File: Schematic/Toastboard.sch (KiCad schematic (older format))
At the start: 46 parts, among them J1 Conn_01x20_Female, J2 USB_B_Micro, Q1 FDS6892A, SW1 SW_Push, SW2 SW_Push, SW3 SW_Push, SW4 SW_Push, SW5 SW_DIP_x04, U1 24LC01, U2 PCT2075D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

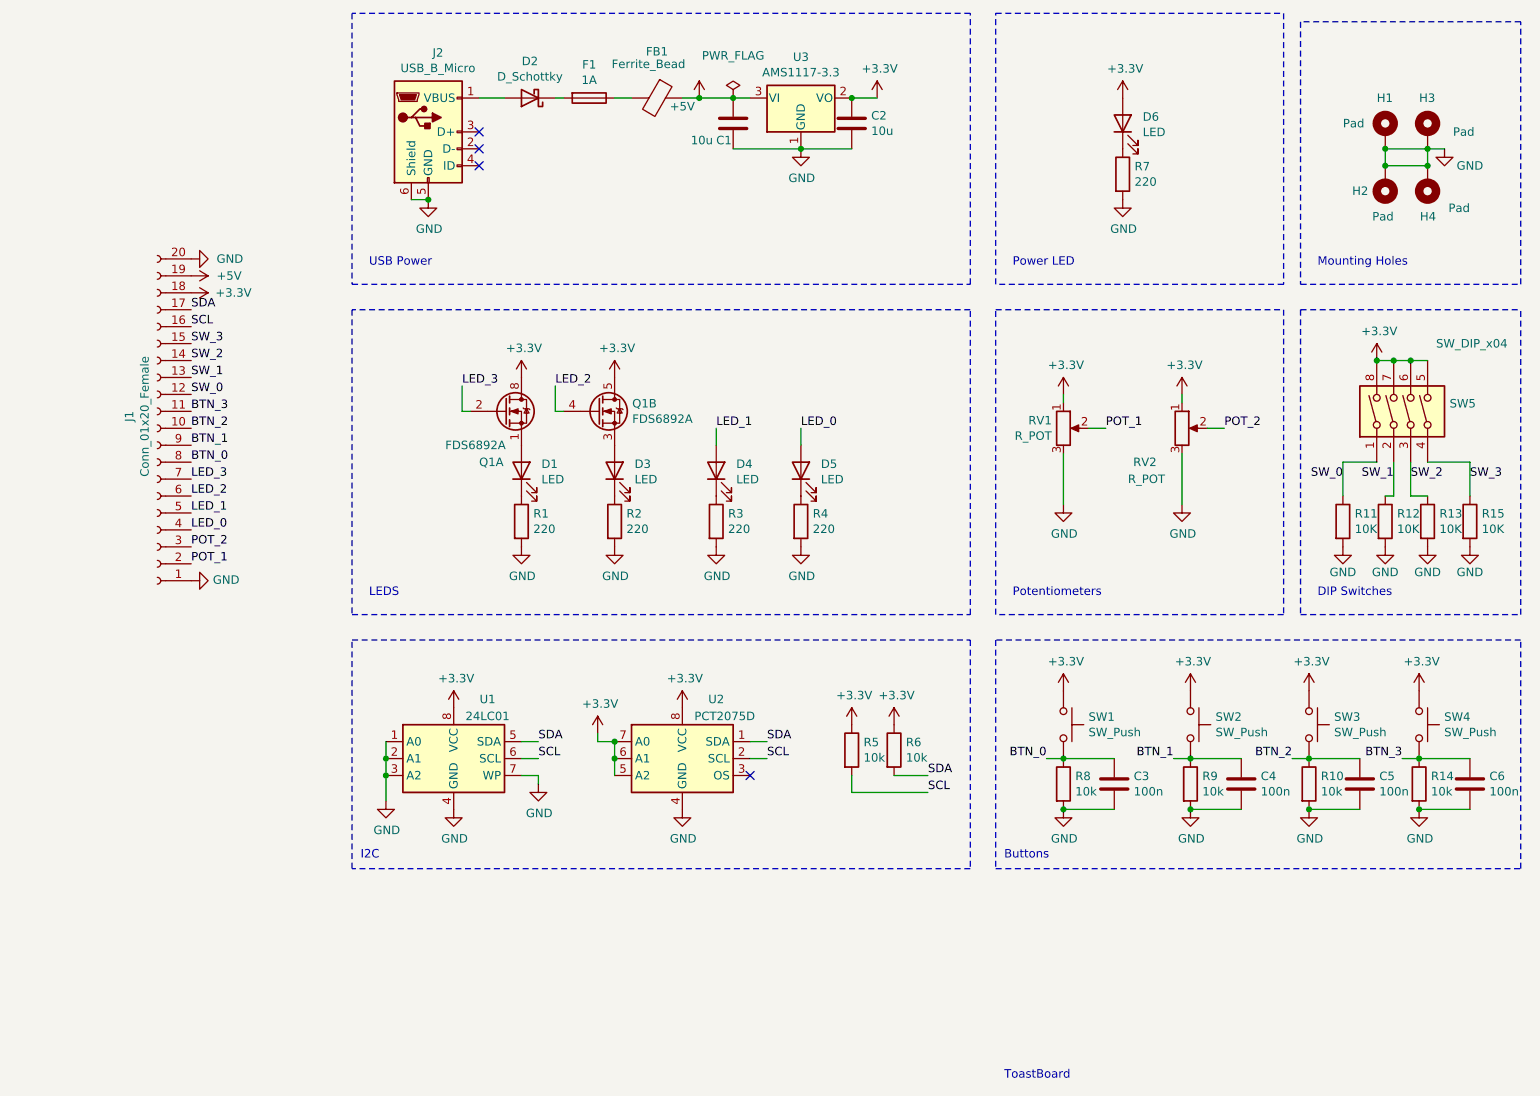
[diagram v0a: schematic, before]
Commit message: Increased via size. Added JLC tracking number
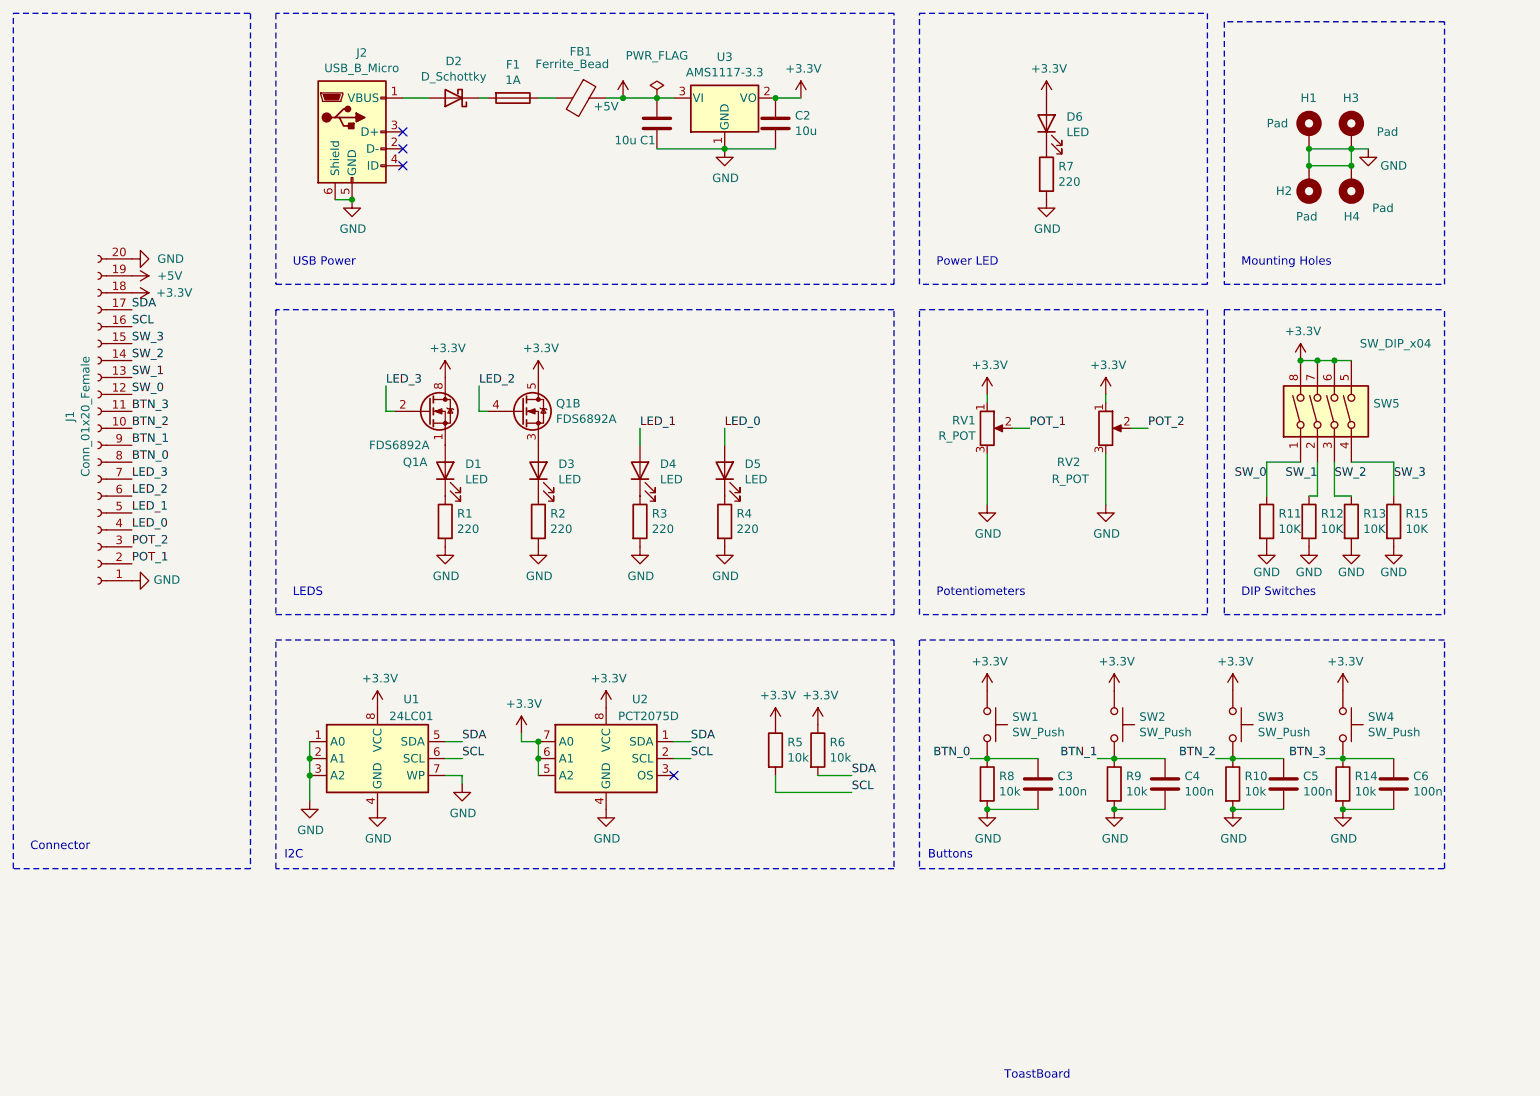
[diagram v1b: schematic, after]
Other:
- note added: "Connector"
- moved on the sheet: C1, C2, C3, C4, C5, C6, D1, D2, D3, D4, D5, D6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

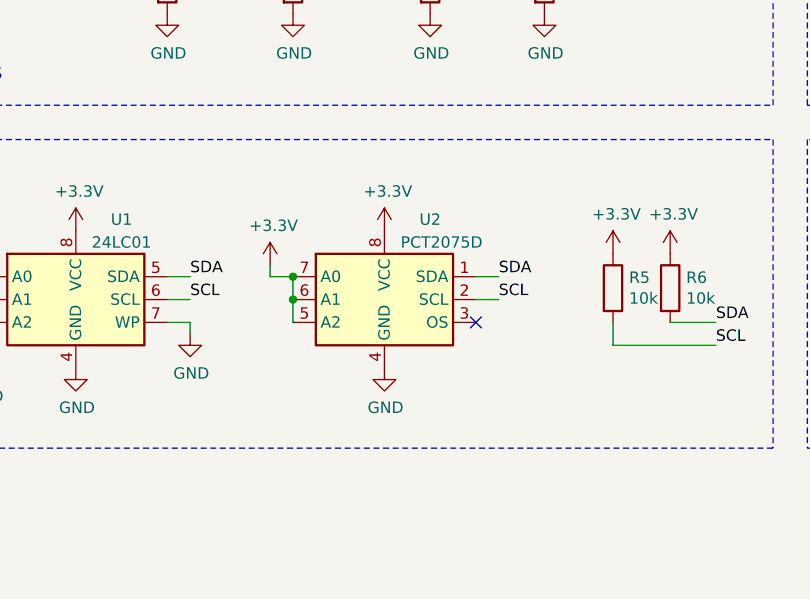
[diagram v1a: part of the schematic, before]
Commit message: Change footprints to match available parts
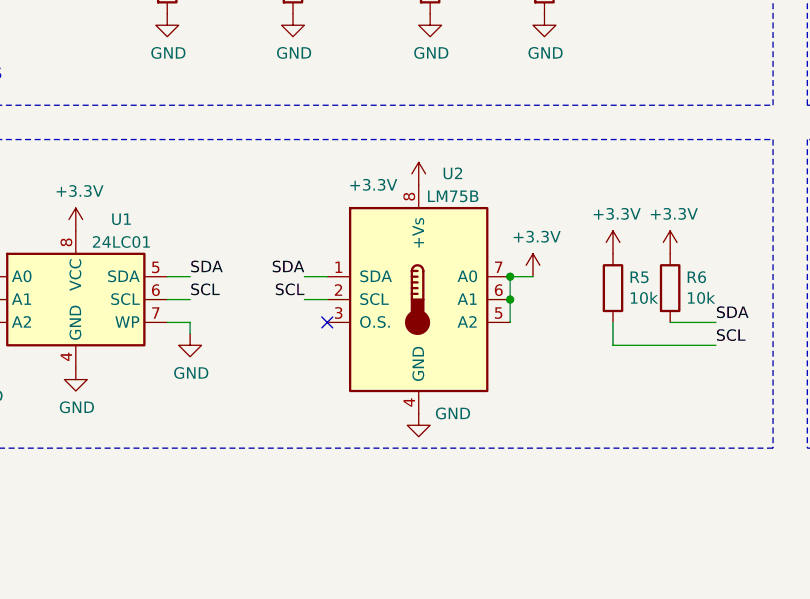
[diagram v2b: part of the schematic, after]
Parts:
- removed U2: PCT2075D, Package_SO:SO-8_3.9x4.9mm_P1.27mm, symbol Sensor_Temperature:PCT2075D
- added U2: LM75B, Package_SO:SOIC-8_3.9x4.9mm_P1.27mm, symbol Sensor_Temperature:LM75B
- D2: footprint Diode_SMD:D_0603_1608Metric_Pad1.05x0.95mm_HandSolder -> Diode_SMD:D_SOD-123
- RV1: footprint Potentiometer_THT:Potentiometer_Vishay_248GJ-249GJ_Single_Vertical -> Potentiometer_THT:Potentiometer_Piher_PC-16_Single_Vertical
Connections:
- net +3V3: now also U2.5 (A2), U2.6 (A1), U2.7 (A0), U2.8 (+Vs)
- net GND: now also U2.4 (GND)
- net SCL: now also U2.2 (SCL)
- net SDA: now also U2.1 (SDA)
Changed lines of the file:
@@
 F 0 "RV1" H 7231 3696 50  0000 R CNN
 F 1 "R_POT" H 7231 3605 50  0000 R CNN
-F 2 "Potentiometer_THT:Potentiometer_Vishay_248GJ-249GJ_Single_Vertical" H 7300 3650 50  0001 C CNN
+F 2 "Potentiometer_THT:Potentiometer_Piher_PC-16_Single_Vertical" H 7300 3650 50  0001 C CNN
 F 3 "~" H 7300 3650 50  0001 C CNN
 	1    7300 3650
@@
 	1    0    0    -1
 $EndComp
-Text Label 5550 5500 0    50   ~ 0
+Text Label 4700 5500 2    50   ~ 0
 SDA
 Wire Wire Line
-	5550 5500 5450 5500
-Text Label 5550 5600 0    50   ~ 0
+	4700 5500 4800 5500
+Text Label 4700 5600 2    50   ~ 0
 SCL
 Wire Wire Line
-	5550 5600 5450 5600
+	4700 5600 4800 5600
 $Comp
 L power:+3.3V #PWR0122
 U 1 1 5EF85311
-P 5050 5300
-F 0 "#PWR0122" H 5050 5150 50  0001 C CNN
-F 1 "+3.3V" H 5065 5473 50  0000 C CNN
-F 2 "" H 5050 5300 50  0001 C CNN
-F 3 "" H 5050 5300 50  0001 C CNN
-	1    5050 5300
+P 5200 5100
+F 0 "#PWR0122" H 5200 4950 50  0001 C CNN
+F 1 "+3.3V" H 5000 5100 50  0000 C CNN
+F 2 "" H 5200 5100 50  0001 C CNN
+F 3 "" H 5200 5100 50  0001 C CNN
+	1    5200 5100
 	1    0    0    -1
 $EndComp
@@
 L power:GND #PWR0123
 U 1 1 5EF85C7A
-P 5050 5900
-F 0 "#PWR0123" H 5050 5650 50  0001 C CNN
-F 1 "GND" H 5055 5727 50  0000 C CNN
-F 2 "" H 5050 5900 50  0001 C CNN
-F 3 "" H 5050 5900 50  0001 C CNN
-	1    5050 5900
-	1    0    0    -1
-$EndComp
-$Comp
-L power:+3.3V #PWR0124
-U 1 1 5EF8A5CF
-P 4550 5450
-F 0 "#PWR0124" H 4550 5300 50  0001 C CNN
-F 1 "+3.3V" H 4565 5623 50  0000 C CNN
-F 2 "" H 4550 5450 50  0001 C CNN
-F 3 "" H 4550 5450 50  0001 C CNN
-	1    4550 5450
-	1    0    0    -1
-$EndComp
-Wire Wire Line
-	4550 5450 4550 5500
-Wire Wire Line
-	4550 5500 4650 5500
+P 5200 6100
+F 0 "#PWR0123" H 5200 5850 50  0001 C CNN
+F 1 "GND" H 5350 6100 50  0000 C CNN
+F 2 "" H 5200 6100 50  0001 C CNN
+F 3 "" H 5200 6100 50  0001 C CNN
+	1    5200 6100
+	1    0    0    -1
+$EndComp
 Text Label 4200 5500 0    50   ~ 0
 SDA
@@
 F 0 "D2" H 4150 1483 50  0000 C CNN
 F 1 "D_Schottky" H 4150 1574 50  0000 C CNN
-F 2 "Diode_SMD:D_0603_1608Metric_Pad1.05x0.95mm_HandSolder" H 4150 1700 50  0001 C CNN
+F 2 "Diode_SMD:D_SOD-123" H 4150 1700 50  0001 C CNN
 F 3 "~" H 4150 1700 50  0001 C CNN
 	1    4150 1700
@@
 	1    0    0    -1
 $EndComp
-Connection ~ 4650 5600
-Connection ~ 4650 5500
-Wire Wire Line
-	4650 5600 4650 5500
-Wire Wire Line
-	4650 5700 4650 5600
-$Comp
-L Sensor_Temperature:PCT2075D U2
-U 1 1 5EF8033D
-P 5050 5600
-F 0 "U2" H 5250 5950 50  0000 C CNN
-F 1 "PCT2075D" H 5300 5850 50  0000 C CNN
-F 2 "Package_SO:SO-8_3.9x4.9mm_P1.27mm" H 5050 5600 50  0001 C CNN
-F 3 "https://www.nxp.com/docs/en/data-sheet/PCT2075.pdf" H 5050 5600 50  0001 C CNN
-	1    5050 5600
-	1    0    0    -1
-$EndComp
-NoConn ~ 5450 5700
 Text Notes 6950 6200 0    50   ~ 0
 Buttons\n
@@
 Text Notes 1650 6150 0    50   ~ 0
 Connector
+$Comp
+L Sensor_Temperature:LM75B U2
+U 1 1 5EF3F0A5
+P 5200 5600
+F 0 "U2" H 5350 6150 50  0000 C CNN
+F 1 "LM75B" H 5350 6050 50  0000 C CNN
+F 2 "Package_SO:SOIC-8_3.9x4.9mm_P1.27mm" H 5200 5600 50  0001 C CNN
+F 3 "http://www.ti.com/lit/ds/symlink/lm75b.pdf" H 5200 5600 50  0001 C CNN
+	1    5200 5600
+	1    0    0    -1
+$EndComp
+Wire Wire Line
+	5600 5700 5600 5600
+Connection ~ 5600 5600
+Wire Wire Line
+	5600 5600 5600 5500
+$Comp
+L power:+3.3V #PWR01
+U 1 1 5EF9088A
+P 5700 5500
+F 0 "#PWR01" H 5700 5350 50  0001 C CNN
+F 1 "+3.3V" H 5715 5673 50  0000 C CNN
+F 2 "" H 5700 5500 50  0001 C CNN
+F 3 "" H 5700 5500 50  0001 C CNN
+	1    5700 5500
+	1    0    0    -1
+$EndComp
+Wire Wire Line
+	5700 5500 5600 5500
+Connection ~ 5600 5500
+NoConn ~ 4800 5700
 $EndSCHEMATC
